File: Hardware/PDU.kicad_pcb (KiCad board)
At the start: 4 copper layers, 59 x 50 mm, 147 parts, among them IC1 TPS259830ONRGER, IC2 SiC437AED-T1-GE3, J1 Conn_01x03_MountingPin, J2 FAN, J3 USB_C_Receptacle_USB2.0, J4 Conn_01x02_Male, J5 Conn_01x08_Male, J6 Conn_01x02_Male, J7 XT60PW-M, J8 Conn_01x04_Male, J9 XT60PW-M, Q1 SSM3K15AMFV,L3F, Q2 SI7635DP-T1-GE3, Q3 SI7635DP-T1-GE3, Q5 PXP012-30QLJ, Q6 PXP012-30QLJ, Q7 SQS141ELNW-T1_GE3, Q8 SQS141ELNW-T1_GE3, U1 LTC4412xS6, U10 SC4215, U2 ESP32-S3, U4 MAX77827AEFD+T, U5 SN65HVD230, U6 LTC4412xS6, U7 LTC4412xS6, U8 LTC4412xS6, Y1 40MHz±10ppm

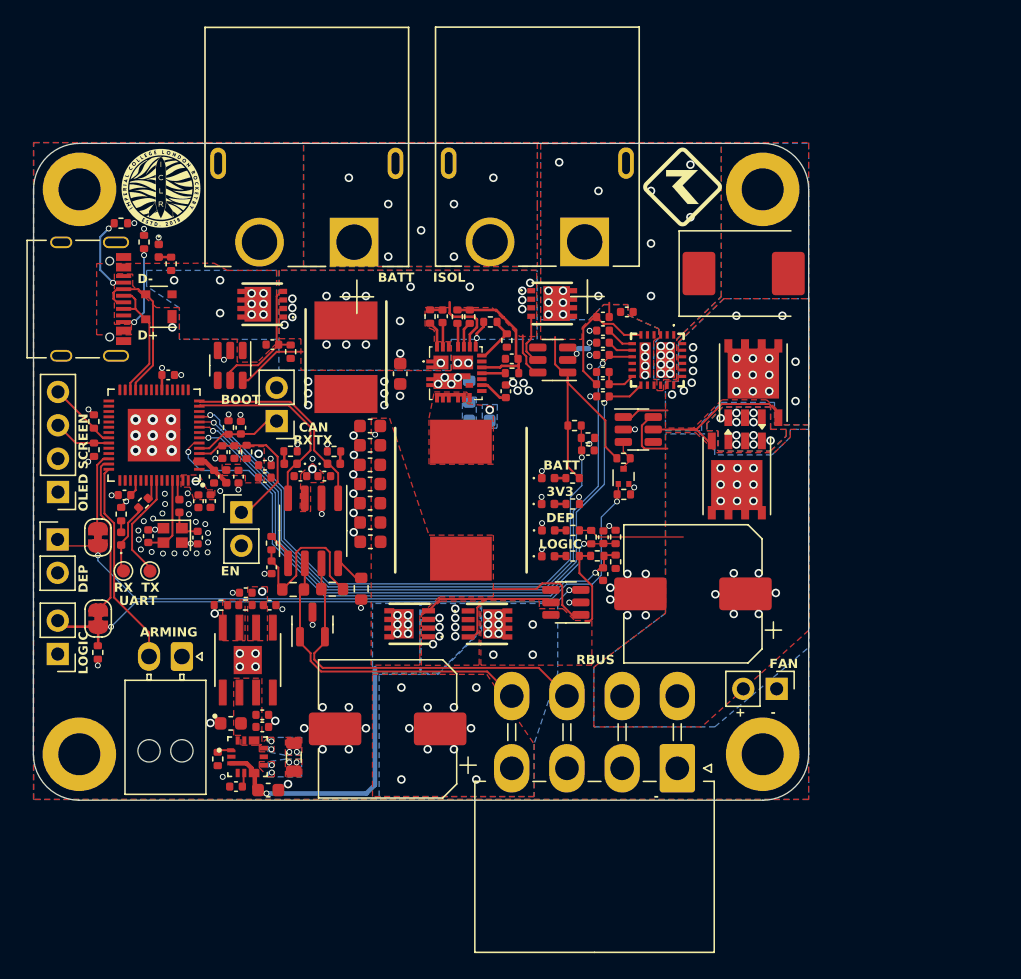
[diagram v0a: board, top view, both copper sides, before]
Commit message: Initial changes : removed efuse in place of a current sensor and hardware fuse xt60
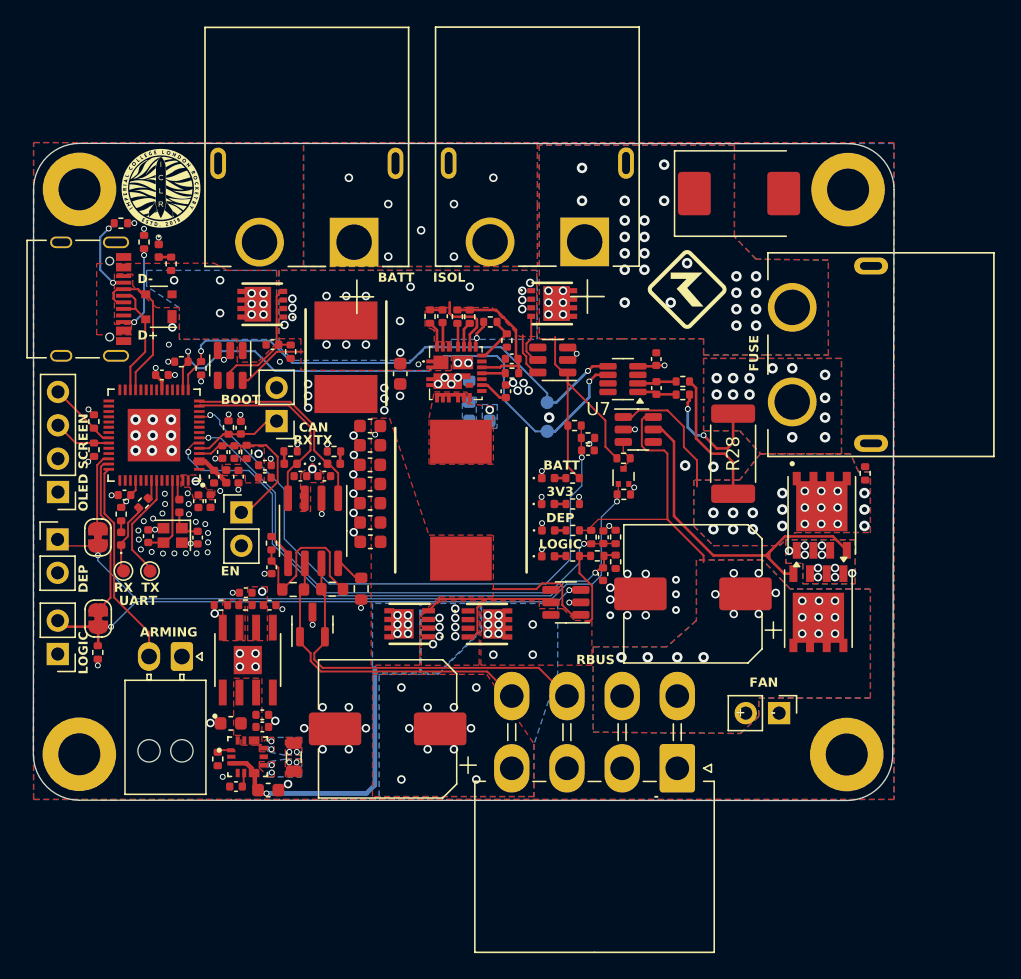
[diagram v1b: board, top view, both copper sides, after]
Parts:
- removed the C21 at (156.8, 84.7)
- removed the C22 at (158.7, 83.3)
- removed the IC1 at (161.0, 86.9)
- removed the R38 at (156.8, 85.6)
- removed the R39 at (156.8, 83.7)
- removed the R40 at (156.8, 88.8)
- removed the R41 at (156.8, 87.8)
- removed the R42 at (156.8, 86.5)
- removed the R43 at (156.8, 89.7)
- added C29: 0.1uF, Capacitor_SMD:C_0402_1005Metric, F.Cu at (160.9, 89.1)
- added C30: 0.1uF, Capacitor_SMD:C_0402_1005Metric, F.Cu at (160.9, 86.9)
- added J8: XT60PW-F, iclr:AMASS_XT60PW-F, F.Cu at (171.2, 86.5)
- added R28: 2m, Resistor_SMD:R_2512_6332Metric_Pad1.40x3.35mm_HandSolder, F.Cu at (166.8, 94.1)
- added R29: 10k, Resistor_SMD:R_0402_1005Metric, F.Cu at (176.8, 95.6)
- added R30: 10, Resistor_SMD:R_0402_1005Metric, F.Cu at (162.9, 89.6)
- added R31: 10, Resistor_SMD:R_0402_1005Metric, F.Cu at (162.9, 88.6)
- added R34: 3.3k, Resistor_SMD:R_0402_1005Metric, F.Cu at (124.8, 87.1)
- added R35: 3.3k, Resistor_SMD:R_0402_1005Metric, F.Cu at (126.2, 87.6)
- added TP3: TestPoint, TestPoint:TestPoint_Pad_D1.0mm, B.Cu at (152.6, 92.4)
- added TP4: TestPoint, TestPoint:TestPoint_Pad_D1.0mm, B.Cu at (152.6, 90.2)
- added U7: INA219AxDCN, Package_TO_SOT_SMD:SOT-23-8, F.Cu at (158.4, 88.4)
- moved Q4 11.9 mm to (173.2, 105.9)
- moved Q3 11.4 mm to (173.5, 98.8)
- moved G*** 7.81 mm to (163.2, 81.6)
- moved H3 6.50 mm to (175.5, 74.0)
- moved H4 6.40 mm to (175.4, 117.0)
- moved D4 6.10 mm to (167.2, 74.3)
- moved J7 1.86 mm to (170.2, 113.8)
- moved C12 0.48 mm to (123.3, 88.1)
- renumbered C28 to C1, C9 to C10, C10 to C11, C11 to C12, C17 to C15, C49 to C16, C50 to C17, C51 to C18, C52 to C19, C1 to C2, C53 to C20, C54 to C21, C18 to C22, C19 to C23, C20 to C24, C23 to C25, C24 to C28, C2 to C3, C15 to C31, C25 to C32, C30 to C33, C32 to C34, C34 to C35, C38 to C37, C47 to C38, C40 to C39, C3 to C4, C42 to C40, C44 to C41, C46 to C42, C16 to C43, C12 to C44, C4 to C5, C5 to C6, C6 to C7, C7 to C8, C8 to C9, D2 to D1, D1 to D2, IC2 to IC1, J3 to J10, J8 to J2, J9 to J3, J7 to J4, J4 to J5, J5 to J6, J2 to J7, J6 to J9, JP2 to JP1, JP1 to JP2, L5 to L3, L3 to L4, Q7 to Q1, Q8 to Q2, Q2 to Q3, Q3 to Q4, Q1 to Q5, Q5 to Q6, Q6 to Q7, R14 to R1, R9 to R10, R46 to R11, R8 to R12, R1 to R13, R12 to R14, R2 to R15, R13 to R16, R15 to R17, R23 to R18, R16 to R19, R22 to R2, R17 to R20, R18 to R21, R24 to R22, R26 to R23, R33 to R24, R27 to R25, R28 to R26, R32 to R27, R19 to R3, R34 to R32, R35 to R33, R10 to R36, R11 to R37, R20 to R38, R21 to R39, R36 to R4, R25 to R40, R29 to R41, R30 to R42, R31 to R43, R37 to R44, R47 to R45, R3 to R5, R5 to R6, R6 to R7, R7 to R8, R4 to R9, TP5 to TP1, TP4 to TP2, U2 to U1, U4 to U2, U10 to U3, U5 to U4, U6 to U5, U7 to U6, U1 to U8, U8 to U9
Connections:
- net /Switches+RBUS/EFuse_OUT renamed /Switches+RBUS/Fuse_OUT
- U1 pad 10: /DepCurrent -> unconnected-(U1-GPIO5/ADC1_CH4-Pad10)
- U1 pad 15: unconnected-(U2-GPIO10/ADC1_CH9-Pad15) -> /CUR_SENS_SCL
- U1 pad 16: unconnected-(U2-GPIO11/ADC2_CH0-Pad16) -> /CUR_SENS_SDA
- U1 pad 9: /EFuse_PG -> unconnected-(U1-GPIO4/ADC1_CH3-Pad9)
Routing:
- net /DepCurrent: track 55.3 -> 0.00 mm, vias 2 -> 0
- net /EFuse_PG: track 53.3 -> 0.00 mm, vias 2 -> 0
- net /CUR_SENS_SDA: track 0.00 -> 44.0 mm, vias 0 -> 2
- net /CUR_SENS_SCL: track 0.00 -> 39.4 mm, vias 0 -> 2
- net /Switches+RBUS/Fuse_OUT: track 3.57 -> 20.8 mm, vias 19 -> 21
- net Net-(U6-GATE): track 12.9 -> 26.4 mm
- net Net-(IC1-EN/UVLO): track 9.99 -> 0.00 mm
- net Net-(J8-Pad1): track 0.00 -> 9.05 mm, vias 0 -> 15
- net Net-(J6-Pin_5): track 12.8 -> 21.7 mm, vias 15 -> 19
- net /Switches+RBUS/SHNT_IN+: track 0.00 -> 3.00 mm
- net /Switches+RBUS/SHNT_IN-: track 0.00 -> 2.98 mm
- net /Switches+RBUS/OVLO: track 2.93 -> 0.00 mm
- net +3V3: track 8.47 -> 11.2 mm, vias 14 -> 16
- net Net-(IC1-ITIMER): track 2.15 -> 0.00 mm
- net Net-(IC1-ILIM): track 1.98 -> 0.00 mm
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- added copper zone on In1.Cu, net +12V
- added copper zone on In2.Cu, net +12V
- added copper zone on In1.Cu, net /Switches+RBUS/Fuse_OUT
- added copper zone on In2.Cu, net /Switches+RBUS/Fuse_OUT
- added copper zone on In1.Cu, net Net-(J6-Pin_5)
- added copper zone on In2.Cu, net Net-(J6-Pin_5)
- added copper zone on B.Cu, net Net-(J8-Pad1)
- added copper zone on F.Cu, net Net-(J8-Pad1)
- added copper zone on In1.Cu, net Net-(J8-Pad1)
- added copper zone on In2.Cu, net Net-(J8-Pad1)
- added copper zone on In1.Cu, net Net-(Q3-Pad1)
- added copper zone on In2.Cu, net Net-(Q3-Pad1)
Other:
- board size 59 x 50 mm -> 65.5 x 50 mm
- board text added: "FUSE"
- board text added: "SCL"
- board text added: "SDA"

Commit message: feat: Some review updates
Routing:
- net GND: vias 115 -> 117
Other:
- board text added: "Lightning McQueen v3.1"
- board text removed: "Lightning McQueen v3"

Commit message: feat: More board review
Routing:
- net Net-(U6-GATE): track 26.4 -> 27.1 mm
- net Net-(J6-Pin_5): track 21.7 -> 22.2 mm
- net GND: vias 117 -> 116
